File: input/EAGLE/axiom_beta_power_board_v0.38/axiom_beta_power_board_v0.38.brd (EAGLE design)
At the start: 101.6 x 57.1 mm, 329 parts, among them Q1 NX3008NBKT, U1 PIC16F15325-JQ, U10 AP7312-3333W6-7, U11 AP7312-3333W6-7, U12 AP7312-3333W6-7, U13 AP7312-3333W6-7, U14 PAC1720, U15 PAC1720, U16 PAC1720, U17 PAC1720, U18 PAC1720, U19 PAC1720, U2 TPS82130SIL-GM, U20 PAC1720, U21 PAC1720, U22 PAC1720, U23 PAC1720, U24 PAC1720, U25 PCA9306GM, U26 SC202A, U27 TS3A4751, U28 IP4251CZ16-8-TTL, U29 LM75BGD, U3 TPS82130SIL-GM, U30 PCA9306GM, U31 NCP715, U4 PCA9306GM, U5 PCA9306GM, U6 MCP23018-E/MJ, U7 MCP23018-E/MJ, U8 MCP23018-E/MJ, U9 MCP23018-E/MJ, X1 PICO-SPOX-5

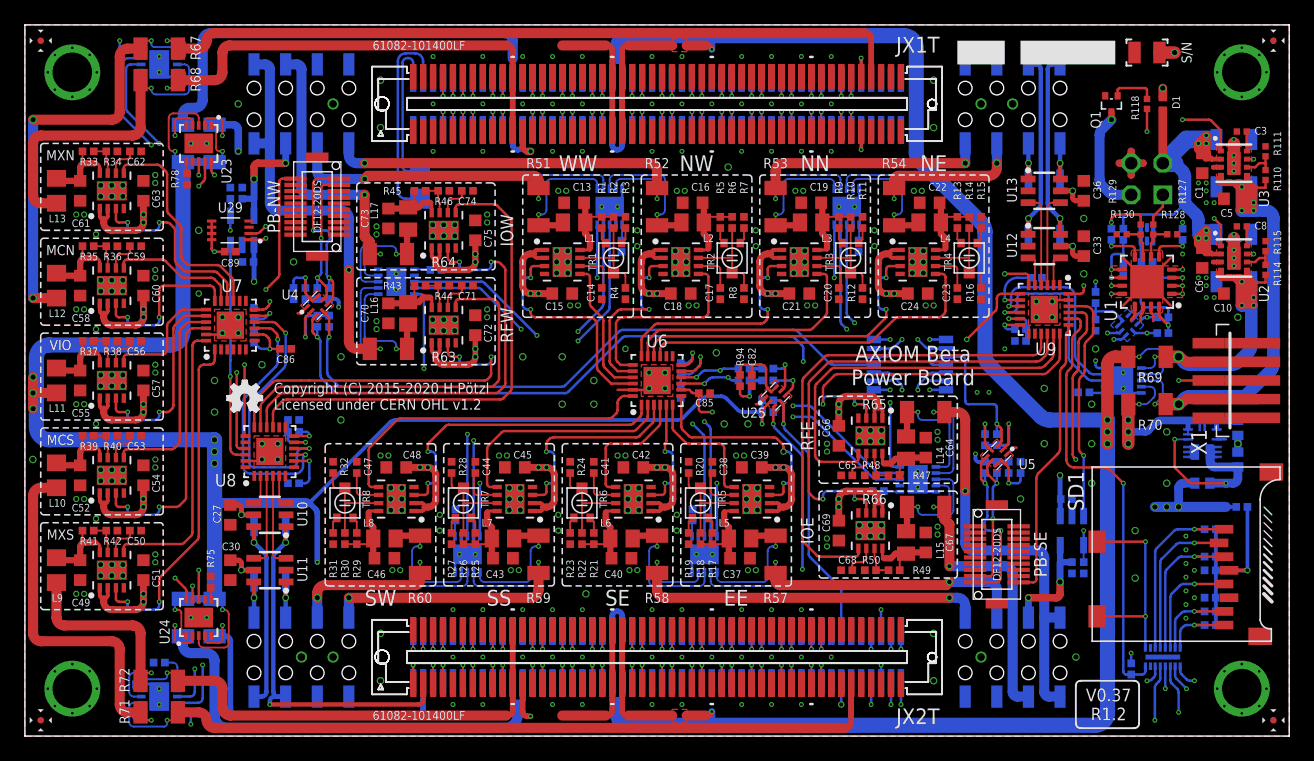
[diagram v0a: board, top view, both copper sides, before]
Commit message: MB & PB V0.38 added
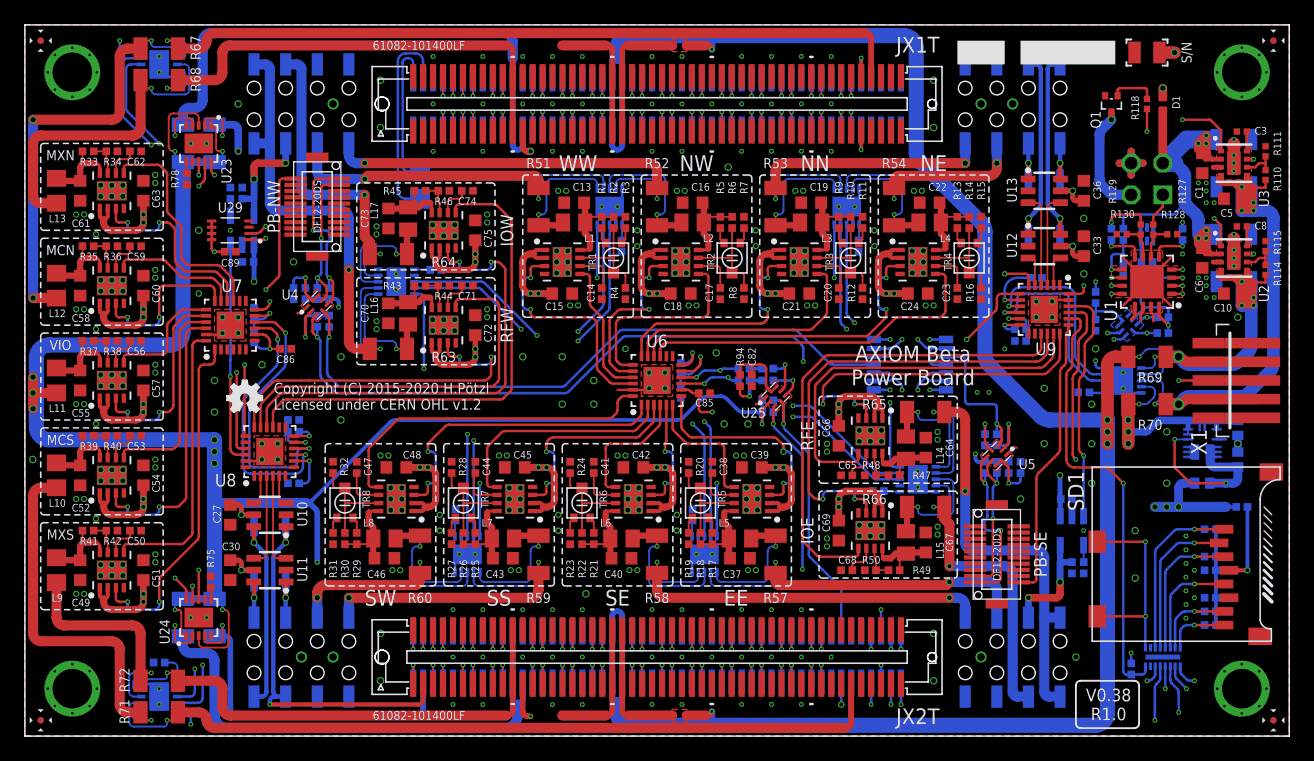
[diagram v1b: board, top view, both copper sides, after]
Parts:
- CNW, CSE: value SPX3819M5-L -> SPX3819M5-L-3-3
- JX1B, JX2B: value BERGSTAK-61083 -> BERGSTAK-61083F; device microzed:61083 -> microzed:61083-FAKE
- JX1T, JX2T: value BERGSTAK-61082 -> BERGSTAK-61082F; device microzed:61082 -> microzed:61082-FAKE
- R110: value 523k -> 147k
- R111, R115: value 100k -> 28k
- R114: value 536k -> 147k
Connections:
- new net CNW_BYP: C76.1, CNW.4
- new net CSE_BYP: C79.1, CSE.4
- net CNW_PG: no longer C76.1, CNW.4
- net CSE_PG: no longer C79.1, CSE.4
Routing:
- net CNW_PG: track 20.8 -> 18.3 mm
- net CSE_PG: track 22.0 -> 19.5 mm
- net CSE_BYP: track 0.00 -> 1.39 mm
- net CNW_BYP: track 0.00 -> 1.39 mm
- net PCIE_I2C_V: track 15.4 -> 14.7 mm
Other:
- board text added: "AXIOM BETA POWER BOARD BOTTOM SIDE V0.38 R1.0"
- board text added: "AXIOM BETA POWER BOARD TOP SIDE V0.38 R1.0"
- board text added: "V0.38 R1.0"
- board text removed: "AXIOM BETA POWER BOARD BOTTOM SIDE V0.37 R1.2"
- board text removed: "AXIOM BETA POWER BOARD TOP SIDE V0.37 R1.2"
- board text removed: "V0.37 R1.2"
